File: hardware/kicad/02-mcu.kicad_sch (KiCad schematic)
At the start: 6 parts, among them U1 ESP32-S3-N16R8

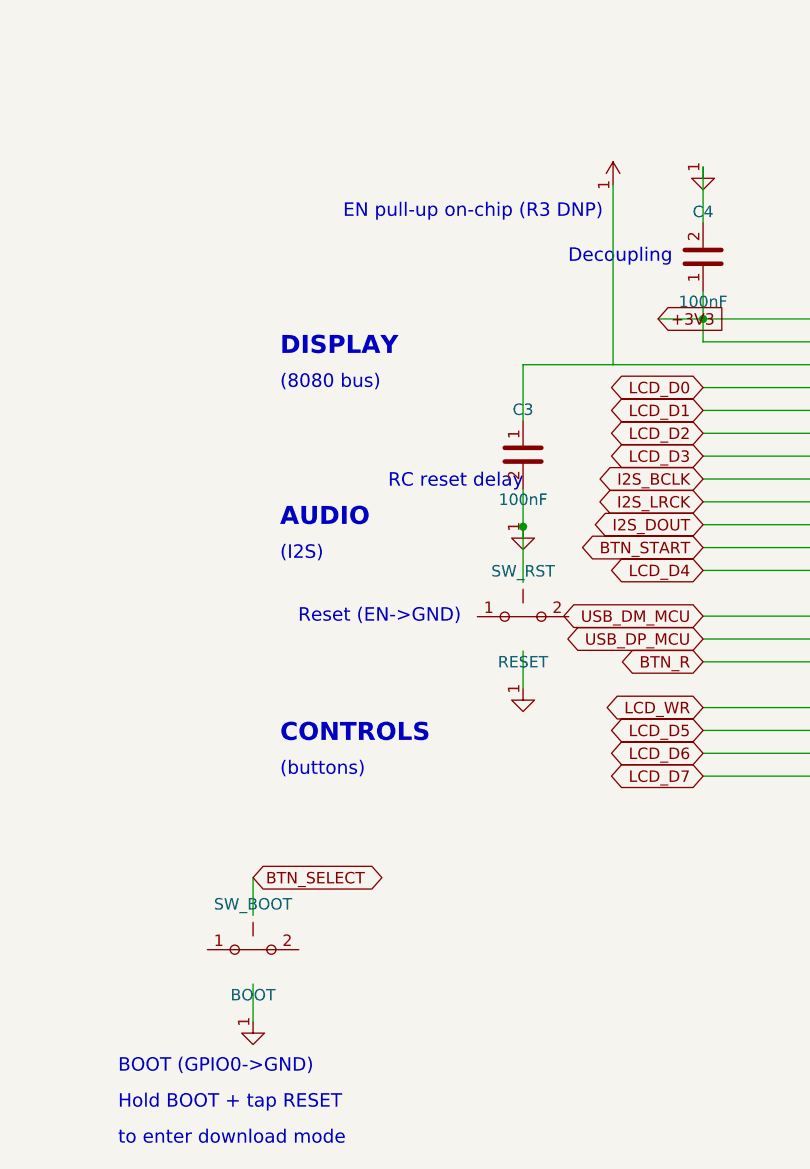
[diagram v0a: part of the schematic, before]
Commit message: sch+routing: EN is its own net, and the reset button was never in the netlist
Recovered in-flight work from a killed session; committed as-is so it can
be reviewed rather than lost. Measured, not asserted: the gate set goes
from 5 red of 6 to 3 red of 6.

SW_Push pins are HORIZONTAL (x +-5.08), not vertical like the R/C
symbols. Wiring the reset and boot buttons the way the passives are wired
put the wires BESIDE the pins: invisible in the plot, and the switches
never reached the netlist at all. That is why no gate had ever compared
them against the PCB.

Fixing the geometry alone would have wired SW_RST across +3V3 and GND,
because the schematic also tied EN straight to the 3V3 rail — so every
press of RESET would have been drawn as a dead short across the rail. The
PCB never had that: EN is its own copper there (T4: U1.3 sch='+3V3'
pcb='EN'). Only the drawing was wrong. EN now carries a global label so it
exports flat as "EN" and matches the PCB net name.

  verify_schematic_pin_connectivity  4 floating -> 0        PASS
  verify_dangling_copper             1 dead end -> 0        PASS
  verify_netlist_diff  T4            7 mismatches -> 1      still FAIL
  verify_net_class_widths            4 undersized -> 2      still FAIL

Two gate changes, both reported and neither suppressing: _LED_MAP is a
pin-vs-pad numbering translation with each side checked independently (a
wrong entry still fails T4), and _buried_in_own_pad exempts a track that
lies wholly inside a pad of its own net, using the pad's INSCRIBED circle
so rotation can never make it exempt more than it should.

Still open here: C3.1 sch='EN' pcb='+3V3' — the routing still ties the
reset cap to the rail.
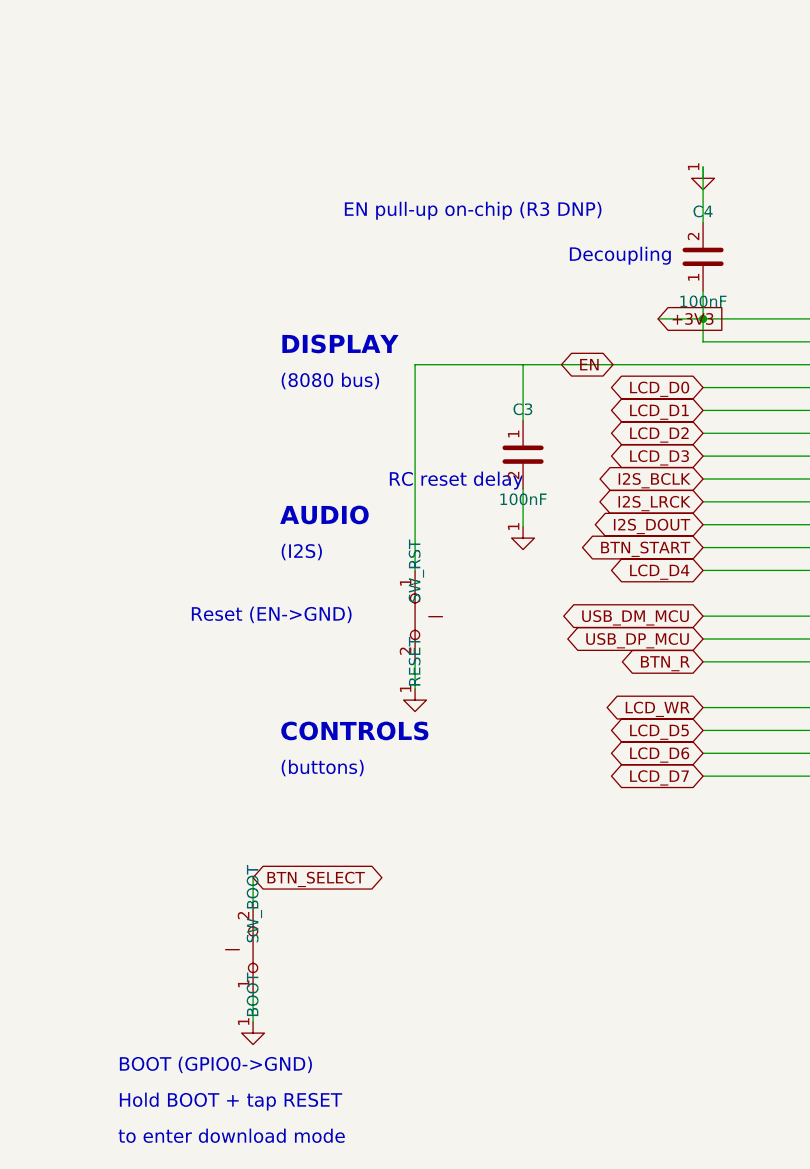
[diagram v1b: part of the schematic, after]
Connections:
- net +3V3: no longer C3.1, U1.3 (EN)
- net BTN_SELECT: now also SW_BOOT.2
- net GND: now also SW_BOOT.1, SW_RST.2
- net EN: now reaches SW_RST.1
- net EN: now also C3.1, U1.3 (EN)

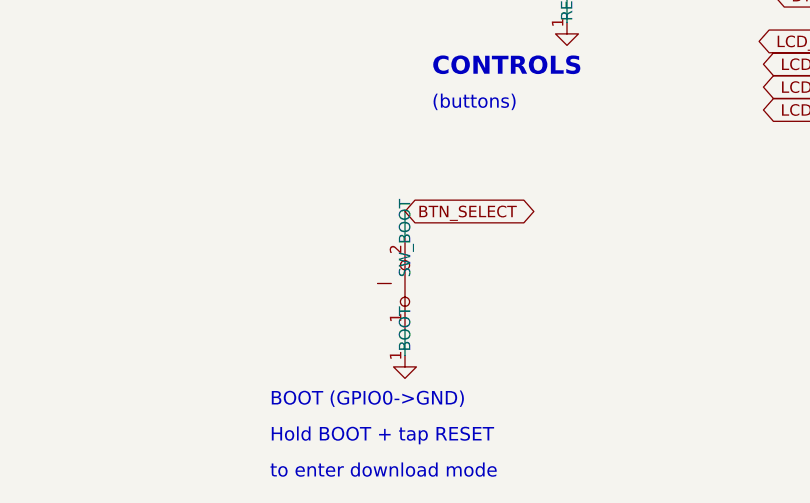
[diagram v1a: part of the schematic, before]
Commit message: sch(SW_BOOT): the signal pole is pads 1/2, so it is symbol pin 1
Salvaged from the killed v25 session, which added SW_RST and SW_BOOT to
SCH_PIN_TO_PCB_PADS. They had never been in that table because their
schematic pins were floating, so no pin of theirs ever reached the
comparison — the gate could not have caught anything about them.

Adding them earned its keep immediately. SW_RST passed, which is
independent confirmation that treating EN as its own net was the right
call. SW_BOOT failed: this side had it at angle=90, putting GND on the
signal pole and BTN_SELECT on the ground pole.

That came from reading "routing.py drives BTN_SELECT onto pad 2" and
reaching for pin 2. A tact switch has two POLES, not four terminals —
pads 1+2 are one, pads 3+4 the other, and the symbol has one pin per pole
(_TACT_MAP). Pad 2 belongs to the pole that is symbol pin 1. The part is
symmetric so the button still shorted GPIO0 to ground either way; what
was wrong was the schematic disagreeing with the board about which pole
is which.

  T4  1 mismatch, unchanged in count but over two more parts than before
  verify_schematic_pin_connectivity  338 pins, 0 floating   PASS

Still open: C3.1 sch='EN' pcb='+3V3'. The schematic draws the RC reset
delay from EN; the PCB ties that cap to the 3V3 rail, so on the board
there is no RC on EN at all — C3 is just another decoupling cap. Left
for a decision, not patched blind: fixing it is a routing change and the
board is already fabricated.
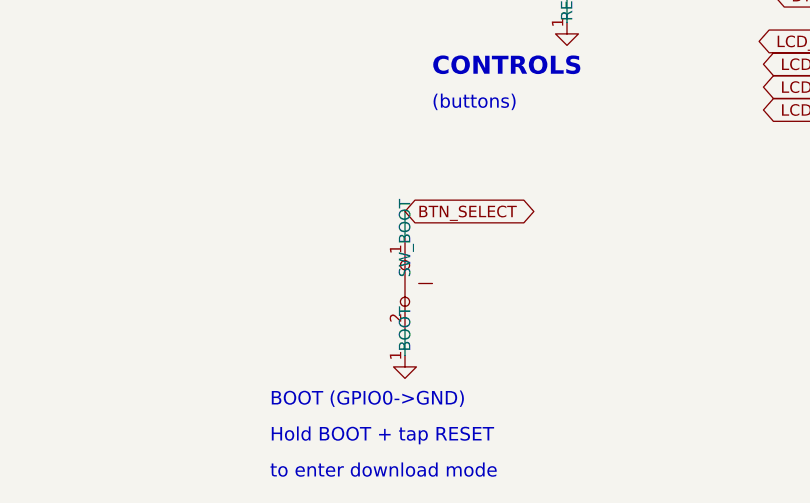
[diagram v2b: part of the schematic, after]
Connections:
- net BTN_SELECT: now also SW_BOOT.1; no longer SW_BOOT.2
- net GND: now also SW_BOOT.2; no longer SW_BOOT.1
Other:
- moved on the sheet: SW_BOOT
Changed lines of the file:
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@@
   (wire (pts (xy 137.76 170.06) (xy 137.76 172.98)) (stroke (width 0) (type default)))
   (text "Reset (EN->GND)" (at 112.75999999999999 164.98 0) (effects (font (size 1.5 1.5)) (justify left)))
-  (symbol (lib_id "SW_Push") (at 119.75999999999999 201.98 90) (unit 1) (exclude_from_sim no) (in_bom yes) (on_board yes) (dnp no) (property "Reference" "SW_BOOT" (at 119.75999999999999 196.932 0) (effects (font (size 1.27 1.27)))) (property "Value" "BOOT" (at 119.75999999999999 207.028 0) (effects (font (size 1.27 1.27)))) (pin "1") (pin "2") (instances (project "esp32-emu-turbo" (path "/00000003-cafe-4000-8000-000000000003" (reference "SW_BOOT") (unit 1)))))
+  (symbol (lib_id "SW_Push") (at 119.75999999999999 201.98 270) (unit 1) (exclude_from_sim no) (in_bom yes) (on_board yes) (dnp no) (property "Reference" "SW_BOOT" (at 119.75999999999999 196.932 0) (effects (font (size 1.27 1.27)))) (property "Value" "BOOT" (at 119.75999999999999 207.028 0) (effects (font (size 1.27 1.27)))) (pin "1") (pin "2") (instances (project "esp32-emu-turbo" (path "/00000003-cafe-4000-8000-000000000003" (reference "SW_BOOT") (unit 1)))))
   (global_label "BTN_SELECT" (shape bidirectional) (at 119.75999999999999 193.98 0) (effects (font (size 1.27 1.27))) (property "Intersheetrefs" "" (at 0 0 0) (effects (font (size 1.27 1.27)) hide)))
   (wire (pts (xy 119.75999999999999 196.89999999999998) (xy 119.75999999999999 193.98)) (stroke (width 0) (type default)))
